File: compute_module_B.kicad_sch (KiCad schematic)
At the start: 19 parts, among them J14 HDMI_A_1.4, U2 TUSB2046IBVF, U3 TPS2044BD, Y1 HC49USM-FF3F18-6.000MHZ

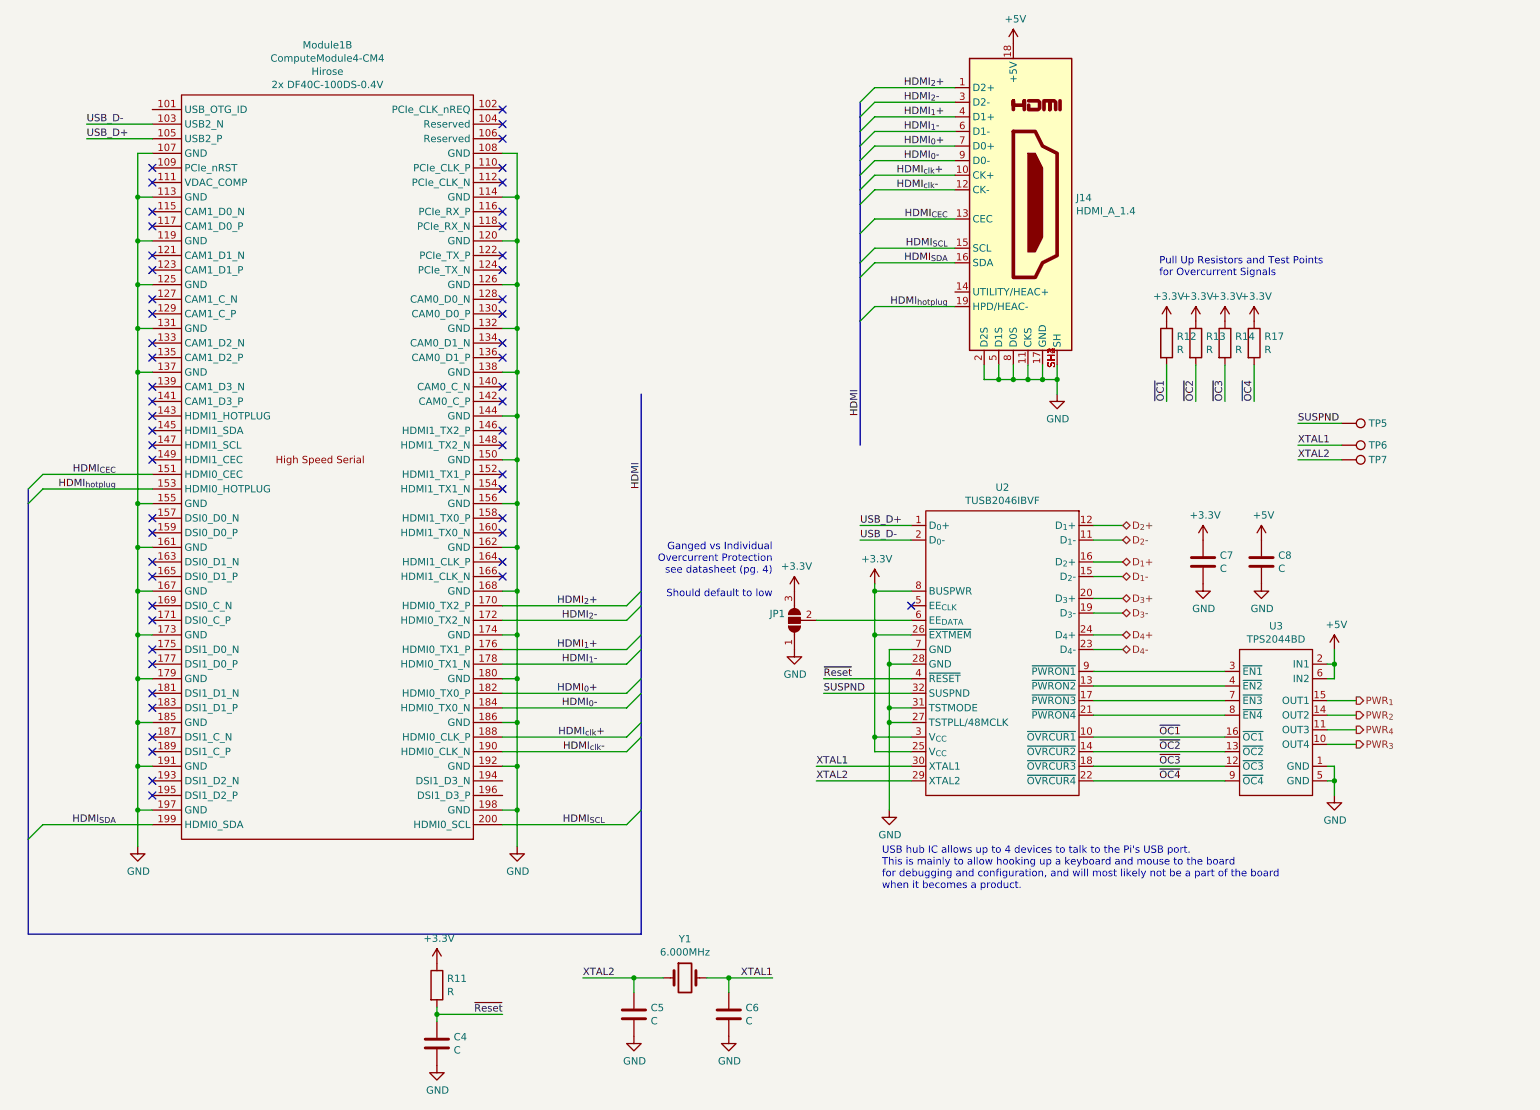
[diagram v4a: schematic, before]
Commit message: Cleaning up
Reassigned reference designators to better match their position on the board.
Moved USB hub IC and related circuits to their own sheet in the schematic.
Tweaked reference designator positions on board to improve visibility.
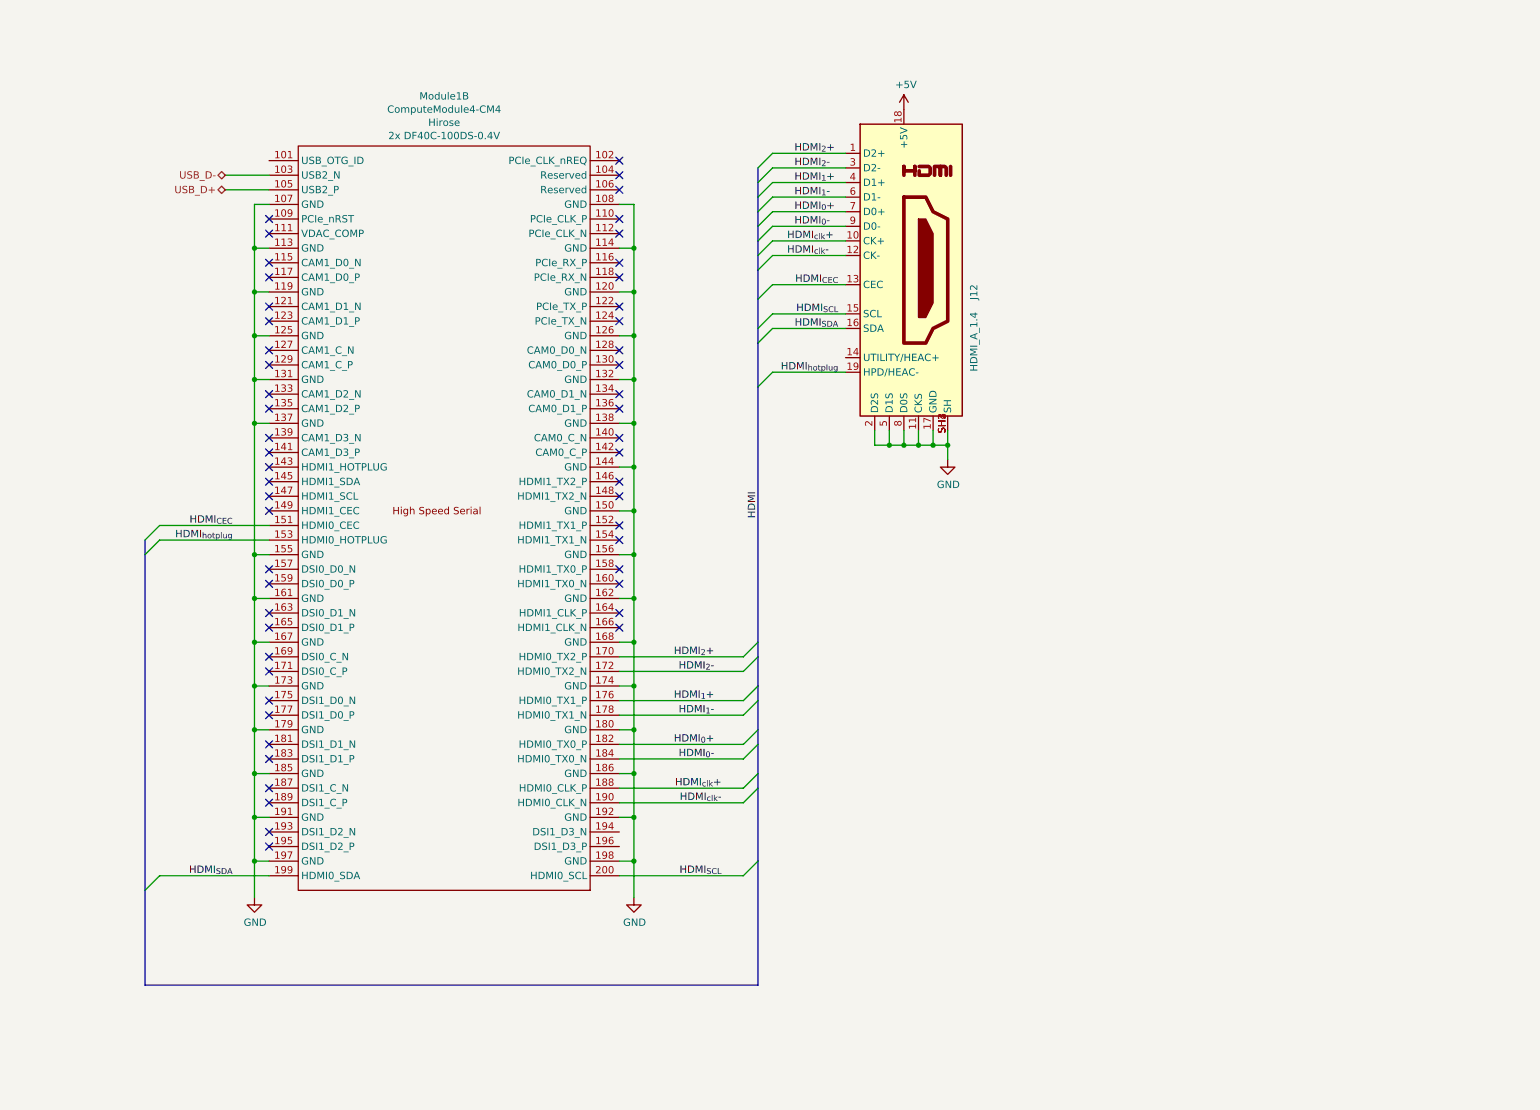
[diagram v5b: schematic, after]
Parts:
- removed C4, C5, C6, C7, C8: C, Capacitor_SMD:C_0805_2012Metric, symbol Device:C
- removed JP1: SolderJumper_3_Open, Jumper:SolderJumper-3_P1.3mm_Open_RoundedPad1.0x1.5mm_NumberLabels, symbol Jumper:SolderJumper_3_Open
- removed R11, R12, R13, R14, R17: R, Resistor_SMD:R_0805_2012Metric, symbol Device:R
- removed TP5, TP6, TP7: TestPoint, TestPoint:TestPoint_Pad_D1.5mm, symbol Connector:TestPoint
- removed U2: TUSB2046IBVF, Package_QFP:LQFP-32_7x7mm_P0.8mm, symbol symbols:TUSB2046IBVF
- removed U3: TPS2044BD, Package_SO:SOIC-16_3.9x9.9mm_P1.27mm, symbol symbols:TPS2044BD
- removed Y1: HC49USM-FF3F18-6.000MHZ, Crystal:Crystal_SMD_HC49-SD, symbol symbols:HC49USM-FF3F18-6.000MHZ
- renumbered J14 to J12
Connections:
- no-connect marks 54 -> 53
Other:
- note removed: "Ganged vs Individual Overcurrent Protection see datasheet (pg. 4) Should default to low"
- note removed: "Pull Up Resistors and Test Points for Overcurrent Signals"
- note removed: "USB hub IC allows up to 4 devices to talk to the Pi's USB port. This is mainly to allow hooking up a keyboard and mouse to the board for debugging and configuration, and will most likely not be a part of the board when it becomes a product."
- moved on the sheet: J12, Module1B

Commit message: migrated computers
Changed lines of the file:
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@@
-(kicad_sch (version 20201015) (generator eeschema)
+(kicad_sch (version 20210621) (generator eeschema)
   (paper "A")
   (title_block
@@
   (junction (at 176.53 90.17) (diameter 0.9144) (color 0 0 0 0))
   (junction (at 179.07 90.17) (diameter 0.9144) (color 0 0 0 0))
+  (no_connect (at 60.96 50.8))
+  (no_connect (at 60.96 53.34))
+  (no_connect (at 60.96 58.42))
+  (no_connect (at 60.96 60.96))
+  (no_connect (at 60.96 66.04))
+  (no_connect (at 60.96 68.58))
+  (no_connect (at 60.96 73.66))
+  (no_connect (at 60.96 76.2))
+  (no_connect (at 60.96 81.28))
+  (no_connect (at 60.96 83.82))
+  (no_connect (at 60.96 88.9))
+  (no_connect (at 60.96 91.44))
+  (no_connect (at 60.96 93.98))
+  (no_connect (at 60.96 96.52))
+  (no_connect (at 60.96 99.06))
+  (no_connect (at 60.96 101.6))
+  (no_connect (at 60.96 111.76))
+  (no_connect (at 60.96 114.3))
+  (no_connect (at 60.96 119.38))
+  (no_connect (at 60.96 121.92))
+  (no_connect (at 60.96 127))
+  (no_connect (at 60.96 129.54))
+  (no_connect (at 60.96 134.62))
+  (no_connect (at 60.96 137.16))
   (no_connect (at 60.96 142.24))
+  (no_connect (at 60.96 144.78))
+  (no_connect (at 60.96 149.86))
+  (no_connect (at 60.96 152.4))
+  (no_connect (at 60.96 157.48))
+  (no_connect (at 60.96 160.02))
+  (no_connect (at 121.92 40.64))
+  (no_connect (at 121.92 43.18))
+  (no_connect (at 121.92 45.72))
+  (no_connect (at 121.92 50.8))
+  (no_connect (at 121.92 53.34))
+  (no_connect (at 121.92 58.42))
+  (no_connect (at 121.92 60.96))
+  (no_connect (at 121.92 66.04))
+  (no_connect (at 121.92 68.58))
+  (no_connect (at 121.92 73.66))
+  (no_connect (at 121.92 76.2))
+  (no_connect (at 121.92 81.28))
+  (no_connect (at 121.92 83.82))
+  (no_connect (at 121.92 88.9))
+  (no_connect (at 121.92 91.44))
+  (no_connect (at 121.92 96.52))
   (no_connect (at 121.92 99.06))
-  (no_connect (at 121.92 60.96))
-  (no_connect (at 60.96 114.3))
-  (no_connect (at 60.96 152.4))
-  (no_connect (at 60.96 101.6))
-  (no_connect (at 121.92 96.52))
-  (no_connect (at 121.92 88.9))
-  (no_connect (at 121.92 50.8))
-  (no_connect (at 60.96 53.34))
-  (no_connect (at 121.92 40.64))
-  (no_connect (at 121.92 81.28))
-  (no_connect (at 60.96 119.38))
+  (no_connect (at 121.92 104.14))
   (no_connect (at 121.92 106.68))
-  (no_connect (at 60.96 149.86))
-  (no_connect (at 121.92 68.58))
-  (no_connect (at 60.96 129.54))
-  (no_connect (at 60.96 91.44))
-  (no_connect (at 60.96 99.06))
+  (no_connect (at 121.92 111.76))
+  (no_connect (at 121.92 114.3))
   (no_connect (at 121.92 119.38))
-  (no_connect (at 60.96 60.96))
-  (no_connect (at 121.92 114.3))
-  (no_connect (at 121.92 104.14))
-  (no_connect (at 121.92 45.72))
-  (no_connect (at 121.92 91.44))
-  (no_connect (at 60.96 83.82))
-  (no_connect (at 60.96 81.28))
-  (no_connect (at 60.96 73.66))
-  (no_connect (at 60.96 121.92))
-  (no_connect (at 121.92 111.76))
-  (no_connect (at 60.96 68.58))
-  (no_connect (at 60.96 88.9))
-  (no_connect (at 60.96 157.48))
-  (no_connect (at 60.96 134.62))
-  (no_connect (at 121.92 76.2))
-  (no_connect (at 121.92 73.66))
-  (no_connect (at 121.92 43.18))
   (no_connect (at 121.92 121.92))
-  (no_connect (at 60.96 111.76))
-  (no_connect (at 60.96 66.04))
-  (no_connect (at 121.92 66.04))
-  (no_connect (at 121.92 58.42))
-  (no_connect (at 60.96 58.42))
-  (no_connect (at 121.92 83.82))
-  (no_connect (at 60.96 137.16))
-  (no_connect (at 60.96 50.8))
-  (no_connect (at 60.96 127))
-  (no_connect (at 60.96 160.02))
-  (no_connect (at 60.96 96.52))
-  (no_connect (at 60.96 144.78))
-  (no_connect (at 121.92 53.34))
-  (no_connect (at 60.96 76.2))
-  (no_connect (at 60.96 93.98))
   (bus_entry (at 39.37 106.68) (size 2.54 -2.54)
     (stroke (width 0.1524) (type solid) (color 0 0 0 0))
@@
     (stroke (width 0) (type solid) (color 0 0 0 0))
   )
-  (bus (pts (xy 39.37 106.68) (xy 39.37 109.22))
-    (stroke (width 0) (type solid) (color 0 0 0 0))
-  )
-  (bus (pts (xy 39.37 109.22) (xy 39.37 167.64))
-    (stroke (width 0) (type solid) (color 0 0 0 0))
-  )
-  (bus (pts (xy 39.37 167.64) (xy 39.37 184.15))
+  (bus (pts (xy 39.37 106.68) (xy 39.37 184.15))
     (stroke (width 0) (type solid) (color 0 0 0 0))
   )
@@
     (stroke (width 0) (type solid) (color 0 0 0 0))
   )
-  (bus (pts (xy 146.05 41.91) (xy 146.05 44.45))
-    (stroke (width 0) (type solid) (color 0 0 0 0))
-  )
-  (bus (pts (xy 146.05 44.45) (xy 146.05 46.99))
-    (stroke (width 0) (type solid) (color 0 0 0 0))
-  )
-  (bus (pts (xy 146.05 46.99) (xy 146.05 49.53))
-    (stroke (width 0) (type solid) (color 0 0 0 0))
-  )
-  (bus (pts (xy 146.05 49.53) (xy 146.05 52.07))
-    (stroke (width 0) (type solid) (color 0 0 0 0))
-  )
-  (bus (pts (xy 146.05 52.07) (xy 146.05 54.61))
-    (stroke (width 0) (type solid) (color 0 0 0 0))
-  )
-  (bus (pts (xy 146.05 54.61) (xy 146.05 57.15))
-    (stroke (width 0) (type solid) (color 0 0 0 0))
-  )
-  (bus (pts (xy 146.05 57.15) (xy 146.05 59.69))
-    (stroke (width 0) (type solid) (color 0 0 0 0))
-  )
-  (bus (pts (xy 146.05 59.69) (xy 146.05 64.77))
-    (stroke (width 0) (type solid) (color 0 0 0 0))
-  )
-  (bus (pts (xy 146.05 64.77) (xy 146.05 69.85))
-    (stroke (width 0) (type solid) (color 0 0 0 0))
-  )
-  (bus (pts (xy 146.05 69.85) (xy 146.05 72.39))
-    (stroke (width 0) (type solid) (color 0 0 0 0))
-  )
-  (bus (pts (xy 146.05 72.39) (xy 146.05 80.01))
-    (stroke (width 0) (type solid) (color 0 0 0 0))
-  )
-  (bus (pts (xy 146.05 80.01) (xy 146.05 124.46))
-    (stroke (width 0) (type solid) (color 0 0 0 0))
-  )
-  (bus (pts (xy 146.05 124.46) (xy 146.05 127))
-    (stroke (width 0) (type solid) (color 0 0 0 0))
-  )
-  (bus (pts (xy 146.05 127) (xy 146.05 132.08))
-    (stroke (width 0) (type solid) (color 0 0 0 0))
-  )
-  (bus (pts (xy 146.05 132.08) (xy 146.05 134.62))
-    (stroke (width 0) (type solid) (color 0 0 0 0))
-  )
-  (bus (pts (xy 146.05 134.62) (xy 146.05 139.7))
-    (stroke (width 0) (type solid) (color 0 0 0 0))
-  )
-  (bus (pts (xy 146.05 139.7) (xy 146.05 142.24))
-    (stroke (width 0) (type solid) (color 0 0 0 0))
-  )
-  (bus (pts (xy 146.05 142.24) (xy 146.05 147.32))
-    (stroke (width 0) (type solid) (color 0 0 0 0))
-  )
-  (bus (pts (xy 146.05 147.32) (xy 146.05 149.86))
-    (stroke (width 0) (type solid) (color 0 0 0 0))
-  )
-  (bus (pts (xy 146.05 149.86) (xy 146.05 162.56))
-    (stroke (width 0) (type solid) (color 0 0 0 0))
-  )
-  (bus (pts (xy 146.05 162.56) (xy 146.05 184.15))
+  (bus (pts (xy 146.05 41.91) (xy 146.05 184.15))
     (stroke (width 0) (type solid) (color 0 0 0 0))
   )
@@
       (effects (font (size 1.27 1.27)) hide)
     )
+    (pin "1")
   )
   (symbol (lib_id "power:GND") (at 58.42 168.91 0) (unit 1)
@@
       (effects (font (size 1.27 1.27)) hide)
     )
+    (pin "1")
   )
   (symbol (lib_id "power:GND") (at 124.46 168.91 0) (unit 1)
@@
       (effects (font (size 1.27 1.27)) hide)
     )
+    (pin "1")
   )
   (symbol (lib_id "power:GND") (at 179.07 92.71 0) (unit 1)
@@
       (effects (font (size 1.27 1.27)) hide)
     )
+    (pin "1")
   )
   (symbol (lib_id "symbols:HDMI_A_1.4") (at 171.45 59.69 0) (unit 1)
@@
       (effects (font (size 1.27 1.27)) hide)
     )
+    (pin "SH2")
+    (pin "SH3")
+    (pin "SH4")
+    (pin "1")
+    (pin "10")
+    (pin "11")
+    (pin "12")
+    (pin "13")
+    (pin "14")
+    (pin "15")
+    (pin "16")
+    (pin "17")
+    (pin "18")
+    (pin "19")
+    (pin "2")
+    (pin "3")
+    (pin "4")
+    (pin "5")
+    (pin "6")
+    (pin "7")
+    (pin "8")
+    (pin "9")
+    (pin "SH1")
   )
   (symbol (lib_id "symbols:ComputeModule4-CM4") (at 231.14 101.6 0) (mirror y) (unit 2)
@@
     (property "Field4" "Hirose" (id 4) (at 91.44 34.0168 0))
     (property "Field5" "2x DF40C-100DS-0.4V" (id 5) (at 91.44 36.3155 0))
+    (pin "101")
+    (pin "102")
+    (pin "103")
+    (pin "104")
+    (pin "105")
+    (pin "106")
+    (pin "107")
+    (pin "108")
+    (pin "109")
+    (pin "110")
+    (pin "111")
+    (pin "112")
+    (pin "113")
+    (pin "114")
+    (pin "115")
+    (pin "116")
+    (pin "117")
+    (pin "118")
+    (pin "119")
+    (pin "120")
+    (pin "121")
+    (pin "122")
+    (pin "123")
+    (pin "124")
+    (pin "125")
+    (pin "126")
+    (pin "127")
+    (pin "128")
+    (pin "129")
+    (pin "130")
+    (pin "131")
+    (pin "132")
+    (pin "133")
+    (pin "134")
+    (pin "135")
+    (pin "136")
+    (pin "137")
+    (pin "138")
+    (pin "139")
+    (pin "140")
+    (pin "141")
+    (pin "142")
+    (pin "143")
+    (pin "144")
+    (pin "145")
+    (pin "146")
+    (pin "147")
+    (pin "148")
+    (pin "149")
+    (pin "150")
+    (pin "151")
+    (pin "152")
+    (pin "153")
+    (pin "154")
+    (pin "155")
+    (pin "156")
+    (pin "157")
+    (pin "158")
+    (pin "159")
+    (pin "160")
+    (pin "161")
+    (pin "162")
+    (pin "163")
+    (pin "164")
+    (pin "165")
+    (pin "166")
+    (pin "167")
+    (pin "168")
+    (pin "169")
+    (pin "170")
+    (pin "171")
+    (pin "172")
+    (pin "173")
+    (pin "174")
+    (pin "175")
+    (pin "176")
+    (pin "177")
+    (pin "178")
+    (pin "179")
+    (pin "180")
+    (pin "181")
+    (pin "182")
+    (pin "183")
+    (pin "184")
+    (pin "185")
+    (pin "186")
+    (pin "187")
+    (pin "188")
+    (pin "189")
+    (pin "190")
+    (pin "191")
+    (pin "192")
+    (pin "193")
+    (pin "194")
+    (pin "195")
+    (pin "196")
+    (pin "197")
+    (pin "198")
+    (pin "199")
+    (pin "200")
   )
 )
